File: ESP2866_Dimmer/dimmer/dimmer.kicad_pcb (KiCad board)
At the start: 2 copper layers, 38 parts, among them J1 Conn_01x04_Male, J2 Screw_Terminal_01x04, J3 Conn_01x03_Male, J5 Screw_Terminal_01x02, J6 Screw_Terminal_01x02, J7 Screw_Terminal_01x02, K1 TIANBO-HJR-4102-L, Q1 2N3904, SW1 SW_Push, U2 LTV-354T, U3 ESP-12E, U4 L78L05_SOT89, U5 LTV-354T, U6 LTV-354T, U7 LTV-354T, U8 LTV-354T

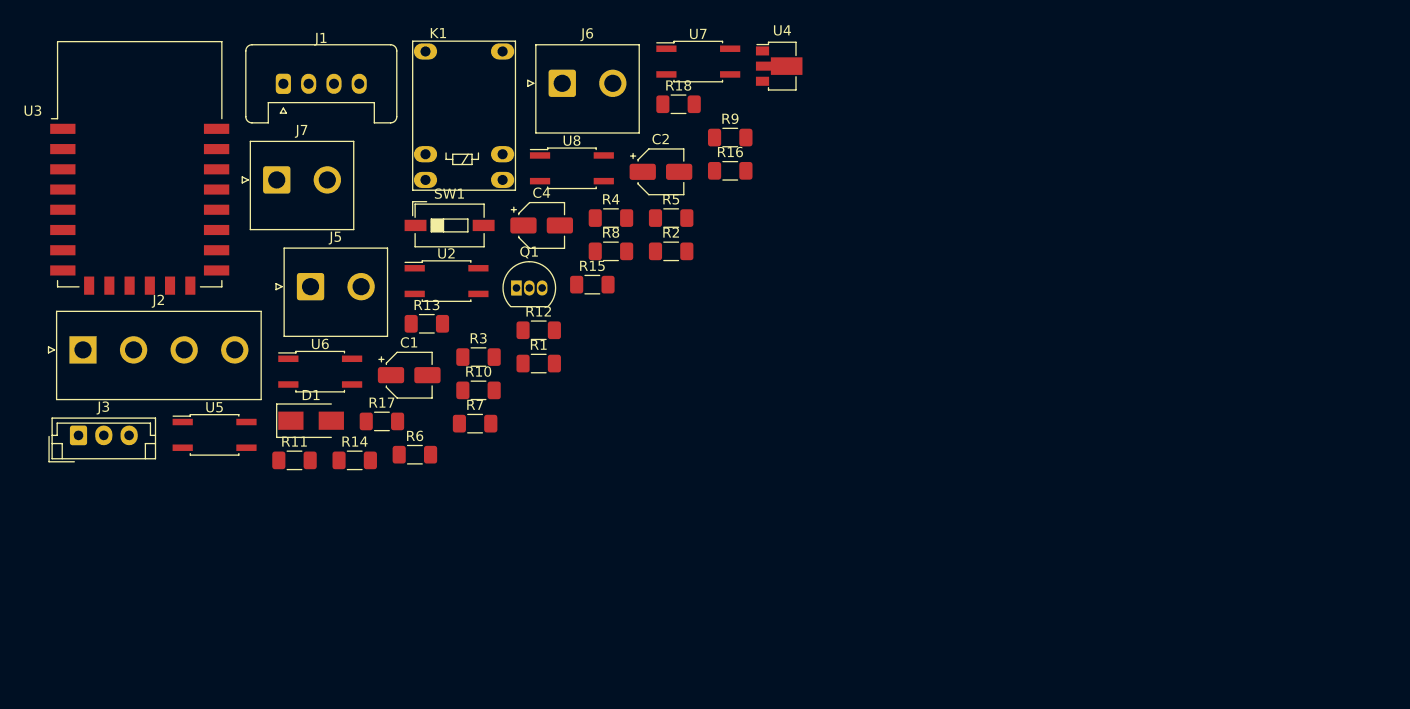
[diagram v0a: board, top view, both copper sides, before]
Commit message: Окремий проект для плати драйверу.
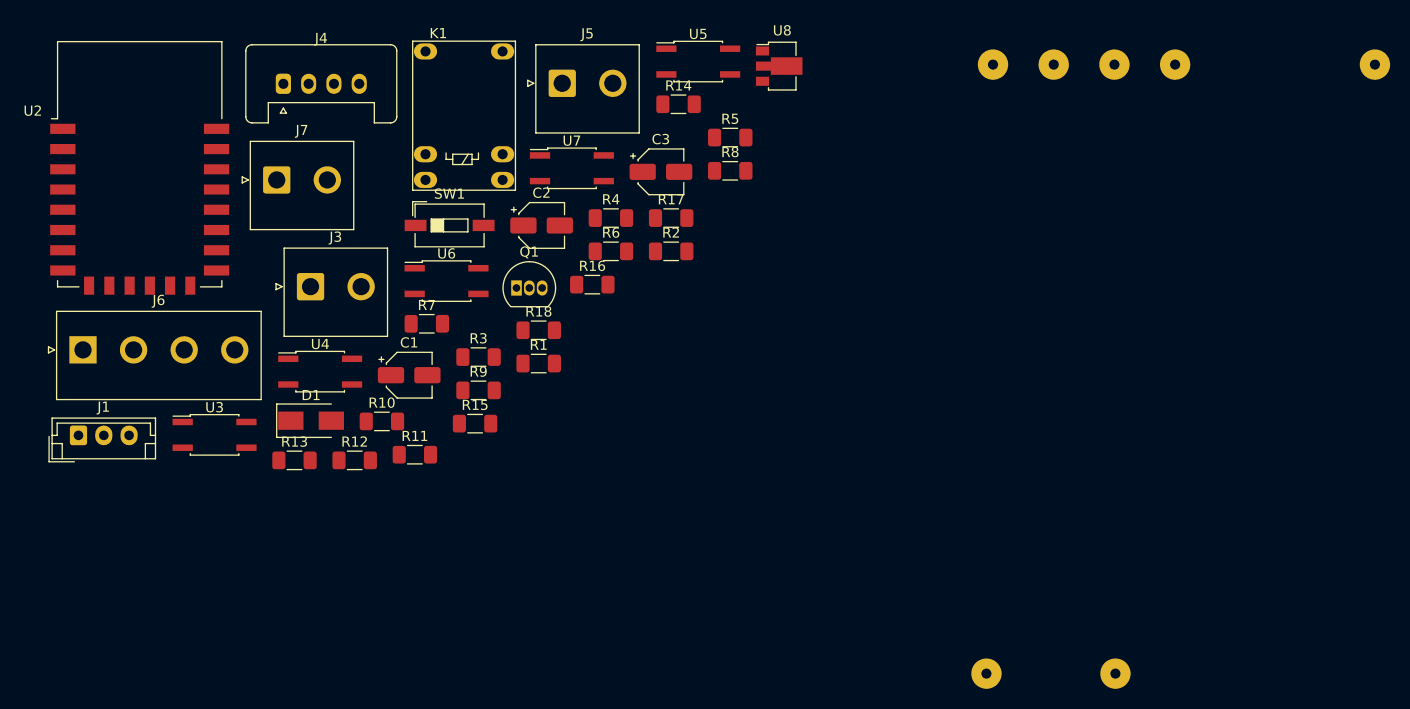
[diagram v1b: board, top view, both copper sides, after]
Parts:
- added U9: LDH-45A-350, dimmer:LDH-45A, B.Cu at (249.9, 50.8)
- renumbered C4 to C2, C2 to C3, J3 to J1, J5 to J3, J1 to J4, J6 to J5, J2 to J6, R17 to R10, R6 to R11, R14 to R12, R11 to R13, R18 to R14, R7 to R15, R15 to R16, R5 to R17, R12 to R18, R9 to R5, R8 to R6, R13 to R7, R16 to R8, R10 to R9, U3 to U2, U5 to U3, U6 to U4, U7 to U5, U2 to U6, U8 to U7, U4 to U8

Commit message: Upd
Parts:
- removed the J5 at (162.4, 60.0)
- removed the U9 at (249.9, 50.8)
- added F1: Fuse, Fuse:Fuse_2920_7451Metric_Pad2.10x5.45mm_HandSolder, F.Cu at (81.5, 39.0)
- added J2: Screw_Terminal_01x02, TerminalBlock_MetzConnect:TerminalBlock_MetzConnect_Type011_RT05502HBWC_1x02_P5.00mm_Horizontal, F.Cu at (141.5, 113.8)
- added R5: 0, Resistor_SMD:R_1206_3216Metric_Pad1.30x1.75mm_HandSolder, F.Cu at (256.8, 109.1)
- added R6: 0, Resistor_SMD:R_1206_3216Metric_Pad1.30x1.75mm_HandSolder, F.Cu at (256.8, 112.4)
- added U1: LDH-45A-350, dimmer:LDH-45A, F.Cu at (96.6, 30.6)
- added U2: B1203S-1WR3, dimmer:B1203-1WR3, F.Cu at (89.5, 103.0)
- J3: value Screw_Terminal_01x02 -> Conn_01x03_Male; footprint Connector_JST:JST_NV_B02P-NV_1x02_P5.00mm_Vertical -> Connector_JST:JST_EH_B3B-EH-A_1x03_P2.50mm_Vertical
- SW1: footprint Button_Switch_SMD:SW_DIP_SPSTx01_Slide_6.7x4.1mm_W6.73mm_P2.54mm_LowProfile_JPin -> Button_Switch_THT:SW_PUSH_6mm
- moved Q1 90.0 mm to (236.5, 124.3)
- moved C3 78.6 mm to (241.0, 106.8)
- moved R15 78.6 mm to (204.8, 135.3)
- moved R18 78.6 mm to (234.2, 117.9)
- moved R3 78.6 mm to (223.0, 125.1)
- moved R8 78.6 mm to (236.1, 114.6)
- moved U9 78.6 mm to (252.7, 96.3)
- moved R11 78.6 mm to (223.0, 128.3)
- moved R14 78.6 mm to (210.8, 135.3)
- moved R4 78.6 mm to (236.1, 111.3)
- moved C1 78.6 mm to (216.1, 126.8)
- moved C2 78.6 mm to (229.2, 112.0)
- moved D1 78.6 mm to (206.4, 131.3)
- moved R1 78.6 mm to (228.9, 125.7)
- moved R10 78.6 mm to (247.9, 106.7)
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- renumbered J6 to J5, J7 to J6, R8 to R10, R9 to R11, R10 to R12, R11 to R13, R12 to R14, R13 to R15, R14 to R16, R15 to R17, R16 to R18, R17 to R19, R18 to R20, R5 to R7, R6 to R8, R7 to R9, U2 to U3, U3 to U4, U4 to U5, U5 to U6, U6 to U7, U7 to U8, U8 to U9
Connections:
- J3 pad 1: Net-(J3-Pad1) -> +3V3
- J3 pad 2: GNDPWR -> /LIGHT_SENSOR
- K1 pad 6: /V12LCD -> Net-(F1-Pad1)
- R7 pad 2: Net-(J3-Pad1) -> Net-(R7-Pad2)
- U4 pad 4: Net-(J3-Pad1) -> Net-(R7-Pad2)

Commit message: робота з друкованною платою
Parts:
- moved U1 101.7 mm to (0.65, 64.4), turned to 90 degrees
- moved J6 93.8 mm to (13.7, 76.5)
- moved J5 90.6 mm to (33.0, 77.0)
- moved J2 88.4 mm to (60.5, 78.2)
- moved U3 64.5 mm to (127.0, 18.0), turned to 0 degrees

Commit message: Update next.
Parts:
- added J6: Screw_Terminal_01x02, Connector_JST:JST_NV_B02P-NV_1x02_P5.00mm_Vertical, F.Cu at (9.00, 1.00)
- J2: footprint TerminalBlock_MetzConnect:TerminalBlock_MetzConnect_Type011_RT05502HBWC_1x02_P5.00mm_Horizontal -> Connector_JST:JST_NV_B02P-NV_1x02_P5.00mm_Vertical
- J5: value Screw_Terminal_01x04 -> Screw_Terminal_01x02; footprint Connector_JST:JST_NV_B04P-NV_1x04_P5.00mm_Vertical -> Connector_JST:JST_NV_B02P-NV_1x02_P5.00mm_Vertical
- moved U4 196.4 mm to (28.5, 10.5)
- moved U5 196.4 mm to (28.0, 2.00)
- moved U6 196.4 mm to (28.0, -15.0)
- moved U7 196.4 mm to (28.0, -24.0)
- moved U8 196.4 mm to (27.5, -6.00)
- moved J2 107.0 mm to (9.00, -15.5), turned to -90 degrees
- moved J7 104.3 mm to (9.05, -27.8), turned to -90 degrees
- moved U1 101.7 mm to (96.6, 30.6), turned to 0 degrees
- moved U2 94.9 mm to (20.1, 38.2)
- moved U3 72.9 mm to (63.0, -17.0), turned to -90 degrees
- moved J5 63.7 mm to (9.00, 18.0), turned to -90 degrees
- renumbered J6 to J7
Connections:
- R20 pad 2: Net-(J5-Pad3) -> Net-(J6-Pad1)
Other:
- board outline added: 101 x 84.1 mm
